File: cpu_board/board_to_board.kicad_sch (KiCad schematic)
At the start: 2 parts

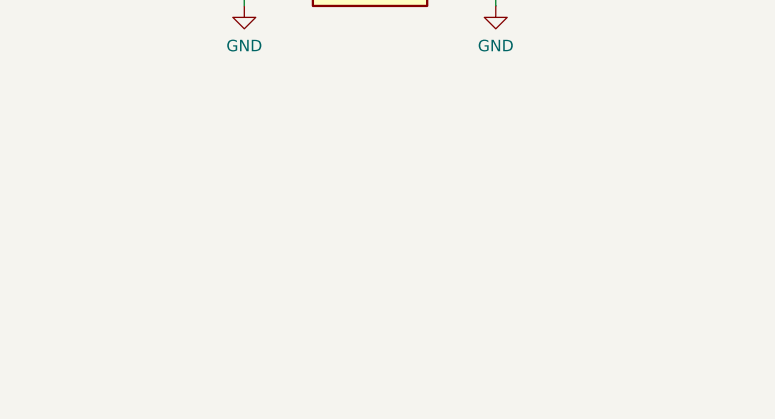
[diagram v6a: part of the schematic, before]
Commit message: clean up silkscreen
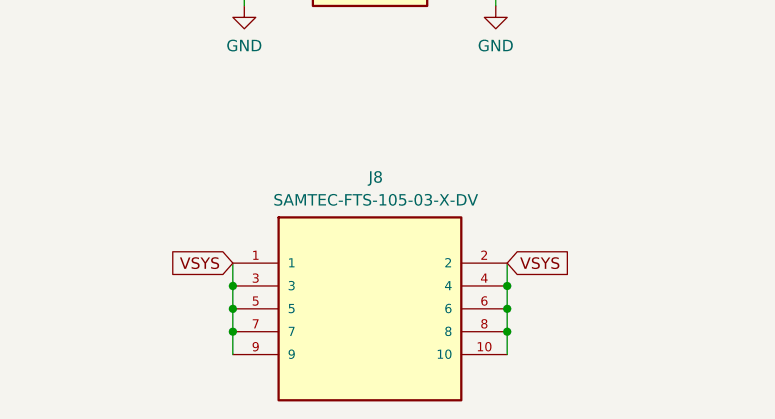
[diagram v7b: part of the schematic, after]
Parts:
- added J8: SAMTEC-FTS-105-03-X-DV, adcs:SAMTEC-FTS-105-03-X-DV, symbol adcs:SAMTEC-FTS-105-03-X-DV
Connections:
- new net VSYS: J8.1, J8.10, J8.2, J8.3, J8.4, J8.5, J8.6, J8.7, J8.8, J8.9
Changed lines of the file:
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@@
   (junction (at 282.575 213.995) (diameter 0) (color 0 0 0 0)
   )
+  (junction (at 128.27 258.445) (diameter 0) (color 0 0 0 0)
+  )
   (junction (at 127 181.61) (diameter 0) (color 0 0 0 0)
   )
@@
   (junction (at 282.575 145.415) (diameter 0) (color 0 0 0 0)
   )
+  (junction (at 128.27 255.905) (diameter 0) (color 0 0 0 0)
+  )
   (junction (at 99.06 217.17) (diameter 0) (color 0 0 0 0)
   )
@@
   (junction (at 124.46 85.09) (diameter 0) (color 0 0 0 0)
   )
+  (junction (at 97.79 253.365) (diameter 0) (color 0 0 0 0)
+  )
   (junction (at 99.06 133.35) (diameter 0) (color 0 0 0 0)
   )
@@
   (junction (at 127 168.91) (diameter 0) (color 0 0 0 0)
   )
+  (junction (at 128.27 253.365) (diameter 0) (color 0 0 0 0)
+  )
   (junction (at 99.06 184.15) (diameter 0) (color 0 0 0 0)
   )
@@
   )
   (junction (at 307.975 84.455) (diameter 0) (color 0 0 0 0)
+  )
+  (junction (at 97.79 258.445) (diameter 0) (color 0 0 0 0)
+  )
+  (junction (at 97.79 255.905) (diameter 0) (color 0 0 0 0)
   )
   (junction (at 127 156.21) (diameter 0) (color 0 0 0 0)
@@
     (stroke (width 0) (type default))
   )
+  (wire (pts (xy 97.79 255.905) (xy 97.79 258.445))
+    (stroke (width 0) (type default))
+  )
   (wire (pts (xy 99.06 171.45) (xy 101.6 171.45))
     (stroke (width 0) (type default))
@@
     (stroke (width 0) (type default))
   )
+  (wire (pts (xy 128.27 255.905) (xy 128.27 258.445))
+    (stroke (width 0) (type default))
+  )
   (wire (pts (xy 129.54 148.59) (xy 124.46 148.59))
     (stroke (width 0) (type default))
@@
     (stroke (width 0) (type default))
   )
+  (wire (pts (xy 97.79 258.445) (xy 97.79 260.985))
+    (stroke (width 0) (type default))
+  )
   (wire (pts (xy 307.975 201.295) (xy 310.515 201.295))
     (stroke (width 0) (type default))
@@
     (stroke (width 0) (type default))
   )
+  (wire (pts (xy 128.27 258.445) (xy 128.27 260.985))
+    (stroke (width 0) (type default))
+  )
   (wire (pts (xy 313.055 127.635) (xy 307.975 127.635))
     (stroke (width 0) (type default))
@@
     (stroke (width 0) (type default))
   )
+  (wire (pts (xy 97.79 253.365) (xy 97.79 255.905))
+    (stroke (width 0) (type default))
+  )
   (wire (pts (xy 313.055 107.315) (xy 307.975 107.315))
     (stroke (width 0) (type default))
@@
     (stroke (width 0) (type default))
   )
+  (wire (pts (xy 128.27 253.365) (xy 128.27 255.905))
+    (stroke (width 0) (type default))
+  )
   (wire (pts (xy 96.52 110.49) (xy 101.6 110.49))
     (stroke (width 0) (type default))
@@
     (stroke (width 0) (type default))
   )
+  (wire (pts (xy 128.27 250.825) (xy 128.27 253.365))
+    (stroke (width 0) (type default))
+  )
   (wire (pts (xy 96.52 176.53) (xy 101.6 176.53))
     (stroke (width 0) (type default))
@@
   )
   (wire (pts (xy 129.54 140.97) (xy 124.46 140.97))
+    (stroke (width 0) (type default))
+  )
+  (wire (pts (xy 97.79 250.825) (xy 97.79 253.365))
     (stroke (width 0) (type default))
   )
@@
     )
   )
+  (global_label "VSYS" (shape input) (at 128.27 250.825 0) (fields_autoplaced)
+    (effects (font (size 1.27 1.27)) (justify left))
+    (property "Intersheetrefs" "${INTERSHEET_REFS}" (at 135.8514 250.825 0)
+      (effects (font (size 1.27 1.27)) (justify left) hide)
+    )
+  )
   (global_label "GPIO_EMC_B2_11" (shape bidirectional) (at 278.765 165.735 180)
     (effects (font (size 1.27 1.27)) (justify right))
@@
     (property "Intersheetrefs" "${INTERSHEET_REFS}" (at 148.3926 120.65 0)
       (effects (font (size 1.27 1.27)) (justify left) hide)
+    )
+  )
+  (global_label "VSYS" (shape input) (at 97.79 250.825 180) (fields_autoplaced)
+    (effects (font (size 1.27 1.27)) (justify right))
+    (property "Intersheetrefs" "${INTERSHEET_REFS}" (at 90.2086 250.825 0)
+      (effects (font (size 1.27 1.27)) (justify right) hide)
     )
   )
@@
         )
       )
+    )
+  )
+  (symbol (lib_id "adcs:SAMTEC-FTS-105-03-X-DV") (at 102.87 250.825 0) (unit 1)
+    (in_bom yes) (on_board yes) (dnp no)
+    (property "Reference" "J8" (at 113.665 241.3 0)
+      (effects (font (size 1.27 1.27)))
+    )
+    (property "Value" "SAMTEC-FTS-105-03-X-DV" (at 113.665 243.84 0)
+      (effects (font (size 1.27 1.27)))
+    )
+    (property "Footprint" "adcs:SAMTEC-FTS-105-03-X-DV" (at 102.87 250.825 0)
+      (effects (font (size 1.27 1.27)) (justify bottom) hide)
+    )
+    (property "Datasheet" "" (at 102.87 250.825 0)
+      (effects (font (size 1.27 1.27)) hide)
+    )
+    (property "DigiKey Part Number" "" (at 102.87 250.825 0)
+      (effects (font (size 1.27 1.27)) hide)
+    )
+    (property "Tolerance" "" (at 102.87 250.825 0)
+      (effects (font (size 1.27 1.27)))
+    )
+    (property "Power Rating" "" (at 102.87 250.825 0)
+      (effects (font (size 1.27 1.27)))
+    )
+    (property "DNI" "DNI" (at 102.87 250.825 0)
+      (effects (font (size 1.27 1.27)) hide)
+    )
+    (pin "1")
+    (pin "10")
+    (pin "2")
+    (pin "3")
+    (pin "4")
+    (pin "5")
+    (pin "6")
+    (pin "7")
+    (pin "8")
+    (pin "9")
+    (instances
+      (project "cpu_board"
+        (path "/c4fd7bdd-408e-44be-b66f-e6a18a0ca6e3/ff5944eb-9859-4dab-aeb3-20c6124220de"
+          (reference "J8") (unit 1)
+        )
+      )

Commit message: update
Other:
- company: (none) -> Stanford Student Space Initiative
- title: (none) -> Soldermander
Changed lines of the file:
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@@
 (kicad_sch (version 20230121) (generator eeschema)
   (paper "A3")
+  (title_block
+    (title "Soldermander")
+    (date "2024-02-27")
+    (rev "1.0")
+    (company "Stanford Student Space Initiative")
+    (comment 1 "RE: Flynn Dreilinger")
+  )
   (junction (at 127 214.63) (diameter 0) (color 0 0 0 0)
   )
